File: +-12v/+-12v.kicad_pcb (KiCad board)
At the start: 2 copper layers, 83.3 x 65 mm, 33 parts, among them J1 Conn_01x04_Male, J2 Conn_01x03_Male, J3 Screw_Terminal_01x02, J4 Screw_Terminal_01x02, U1 LM317_TO3, U2 LM337_TO3

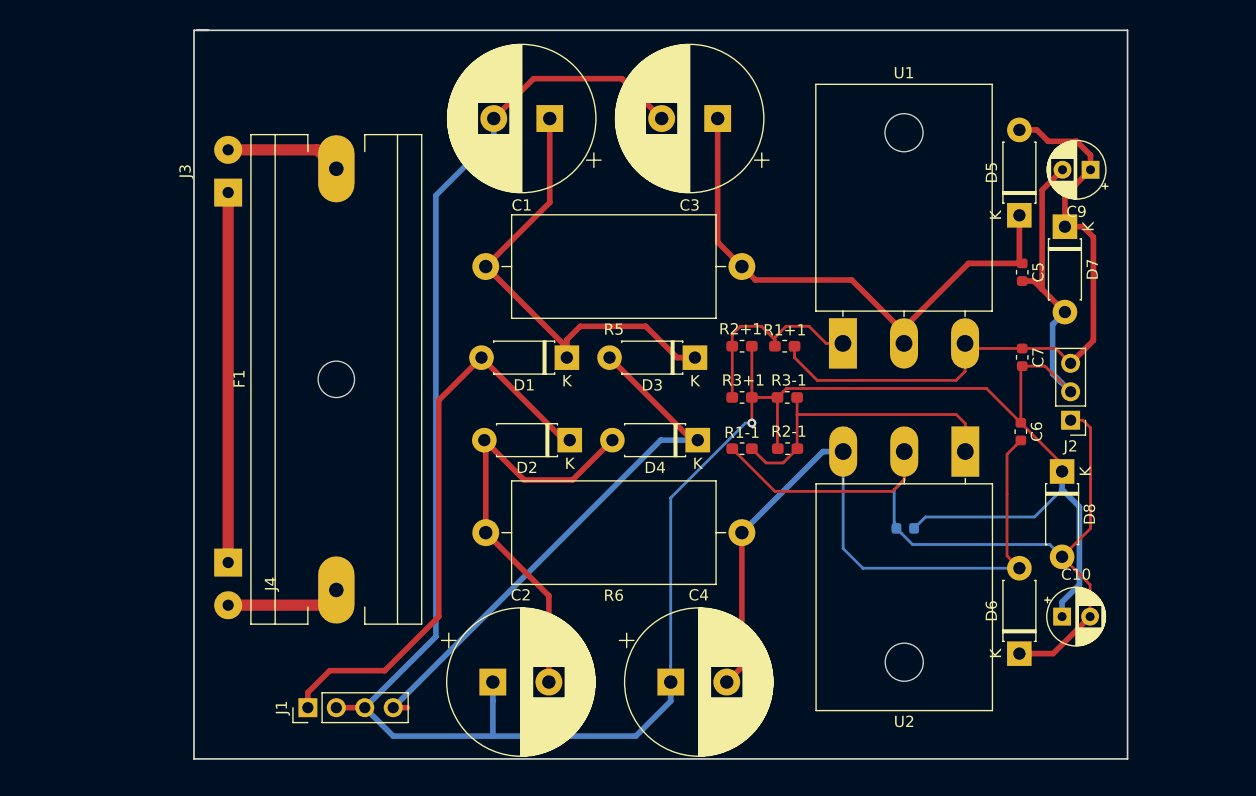
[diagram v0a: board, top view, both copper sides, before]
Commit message: Fix wrong fottprints (the expensive way)
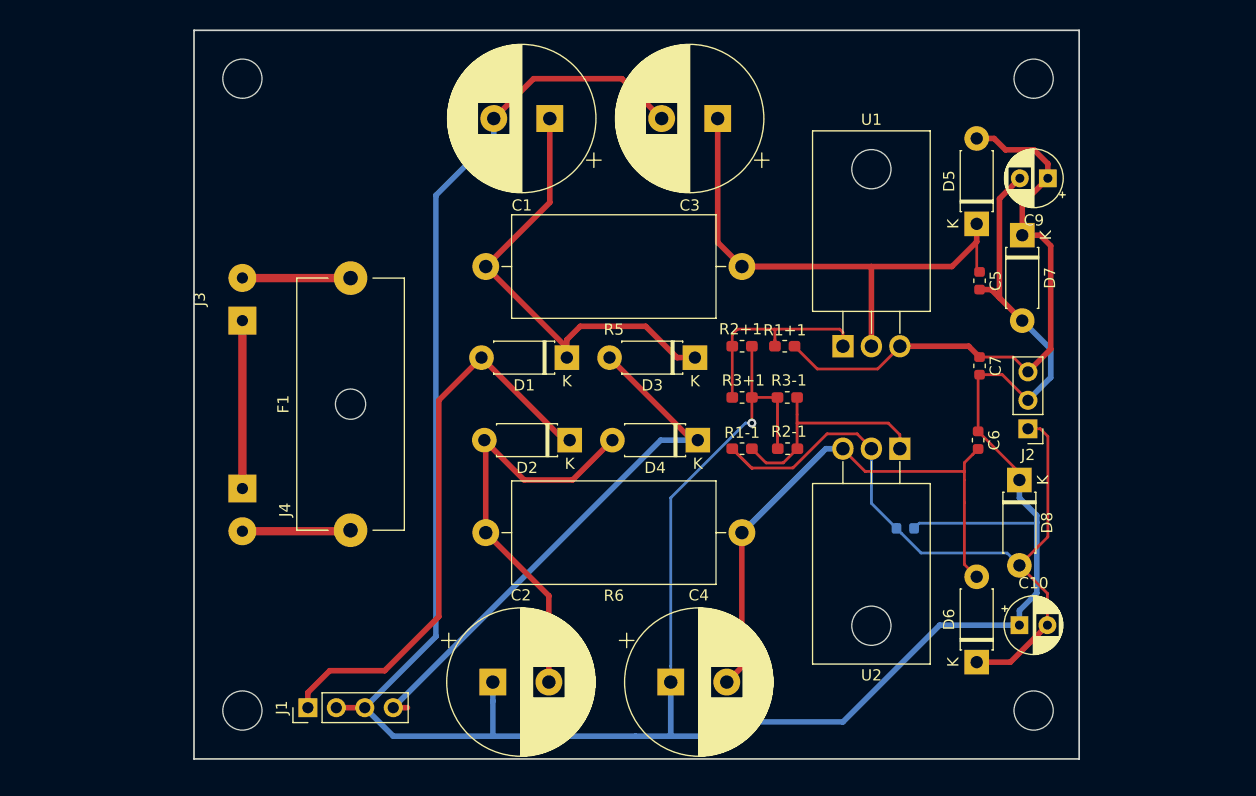
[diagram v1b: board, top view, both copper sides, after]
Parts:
- added REF**: MountingHole_3.5mm, MountingHole:MountingHole_3.5mm, F.Cu at (102.9, 74.4)
- added REF**: MountingHole_3.5mm, MountingHole:MountingHole_3.5mm, F.Cu at (32.3, 74.4)
- added REF**: MountingHole_3.5mm, MountingHole:MountingHole_3.5mm, F.Cu at (32.3, 130.8)
- added REF**: MountingHole_3.5mm, MountingHole:MountingHole_3.5mm, F.Cu at (102.9, 130.8)
- F1: footprint Fuse:Fuseholder_Cylinder-5x20mm_Schurter_0031-8002_Horizontal_Open -> Fuse:Fuseholder_Cylinder-5x20mm_Schurter_0031_8201_Horizontal_Open
- U1, U2: footprint Package_TO_SOT_THT:TO-3P-3_Horizontal_TabDown -> Package_TO_SOT_THT:TO-220F-3_Horizontal_TabDown
- moved J3 11.5 mm to (32.3, 96.0)
- moved J4 6.73 mm to (32.3, 111.0)
- moved U2 5.85 mm to (90.9, 107.4)
- moved F1 5.48 mm to (41.9, 114.7)
- moved C10 3.89 mm to (101.6, 123.2)
- moved C5 3.89 mm to (98.0, 92.5)
- moved C6 3.89 mm to (97.9, 106.7)
- moved C7 3.89 mm to (98.0, 100.1)
- moved C9 3.89 mm to (104.1, 83.3)
- moved D7 3.89 mm to (101.9, 88.4)
- moved D8 3.89 mm to (101.6, 110.2)
- moved J2 3.89 mm to (102.4, 105.7)
- moved D5 3.89 mm to (97.8, 87.4)
- moved D6 3.89 mm to (97.8, 126.5)
- moved U1 0.25 mm to (85.9, 98.3)
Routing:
- net Net-(J3-Pad1): track 33.0 -> 15.0 mm
- net /GND: track 247.2 -> 258.3 mm
- net Net-(R1-1-Pad2): track 27.5 -> 20.6 mm
- net Net-(C7-Pad1): track 59.7 -> 53.1 mm
- net Net-(C10-Pad2): track 71.7 -> 66.9 mm
- net Net-(C3-Pad1): track 50.7 -> 55.3 mm
- net Net-(C4-Pad2): track 63.4 -> 60.3 mm
- net Net-(F1-Pad2): track 10.4 -> 9.66 mm
- net Net-(F1-Pad1): track 10.2 -> 9.69 mm
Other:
- board size 83.3 x 65 mm -> 79 x 65 mm

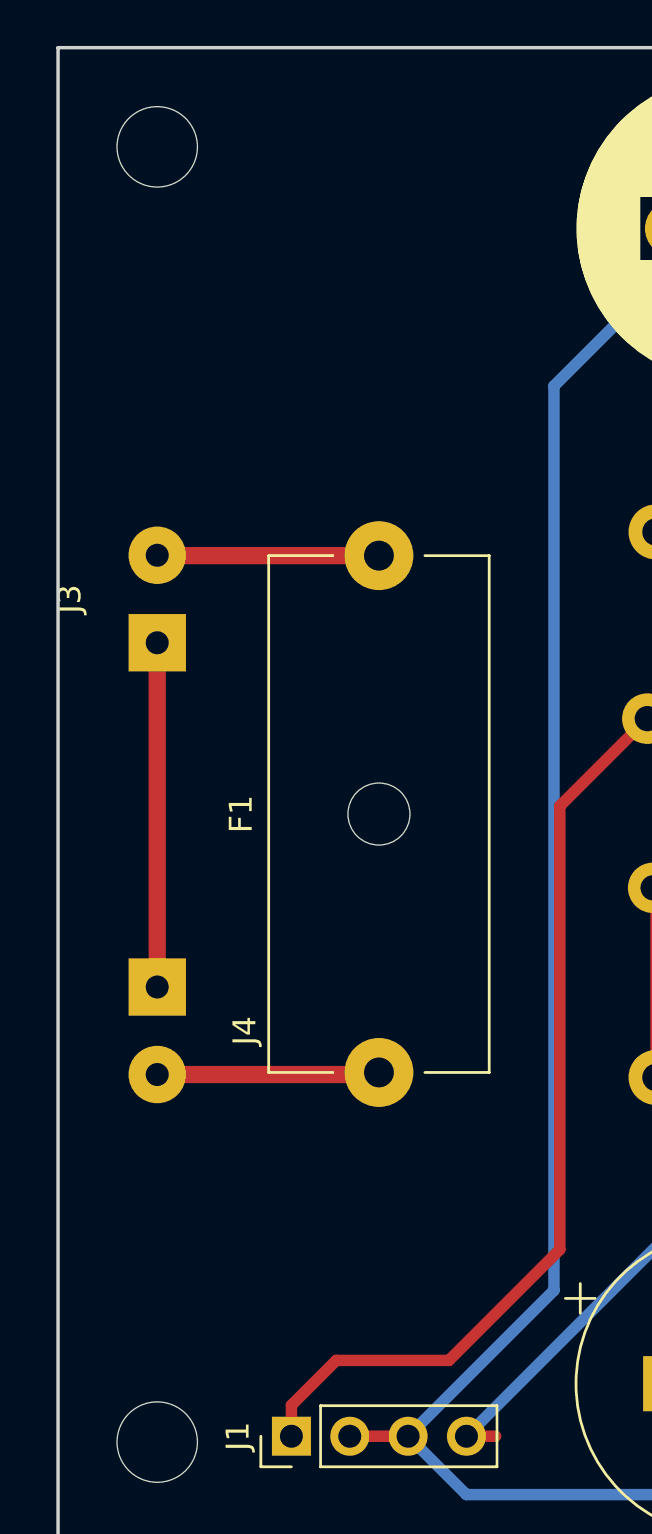
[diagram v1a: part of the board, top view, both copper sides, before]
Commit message: Fix Footprint for Reichelt relay
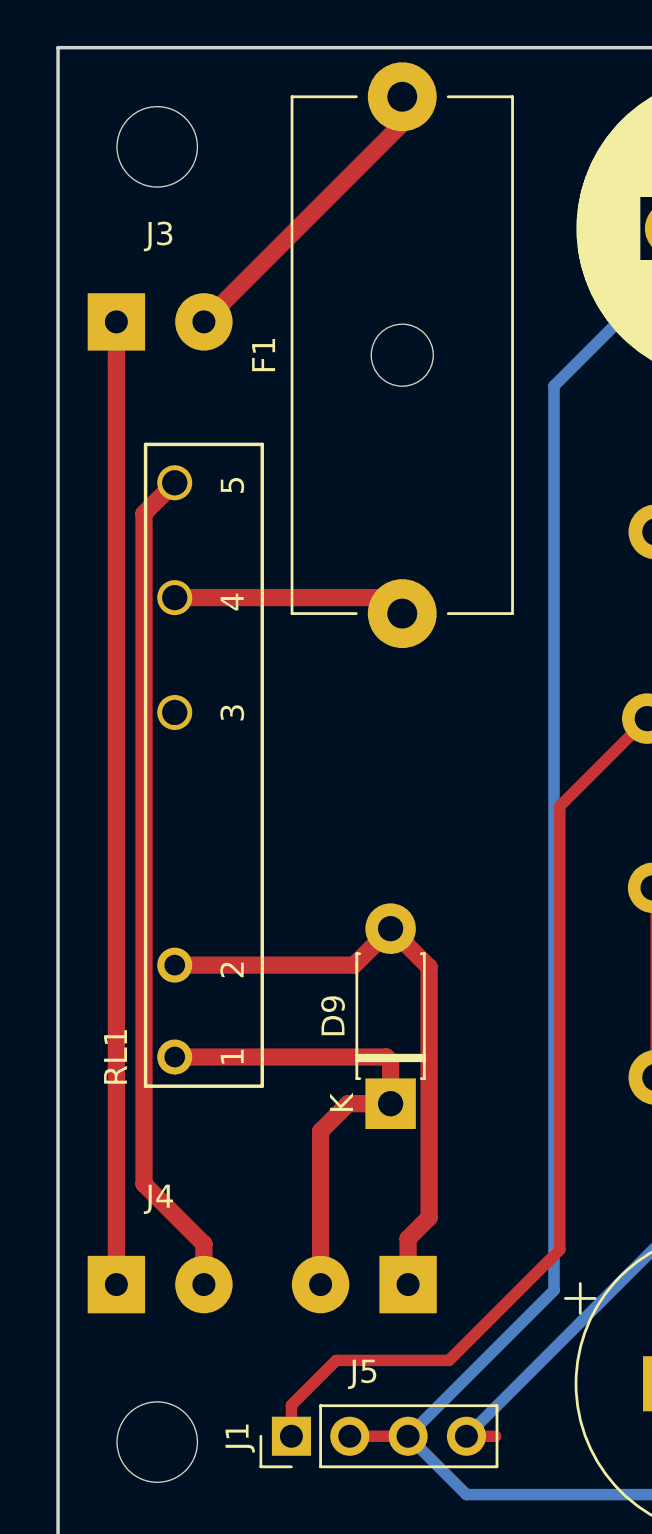
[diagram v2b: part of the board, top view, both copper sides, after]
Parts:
- added D9: D_Small, Diode_THT:D_DO-41_SOD81_P7.62mm_Horizontal, F.Cu at (42.4, 116.1)
- added J5: Screw_Terminal_01x02, Connector_Wire:SolderWirePad_1x02_P3.81mm_Drill1mm, F.Cu at (43.2, 124.0)
- added RL1: FTR-LYCA, lci-kicad:FTR-LYCA, F.Cu at (33.0, 114.0)
- moved F1 20.0 mm to (42.9, 94.7)
- moved J3 14.1 mm to (30.5, 82.0), turned to 0 degrees
- moved J4 13.1 mm to (30.5, 124.0), turned to 0 degrees
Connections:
- J4 pad 2: Net-(F1-Pad1) -> Net-(J4-Pad2)
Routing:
- net Net-(J4-Pad2): track 0.00 -> 36.5 mm
- net Net-(J3-Pad1): track 15.0 -> 41.9 mm
- net Net-(D9-Pad2): track 0.00 -> 26.6 mm
- net Net-(D9-Pad1): track 0.00 -> 21.5 mm
- net Net-(F1-Pad2): track 9.66 -> 15.1 mm
- net Net-(F1-Pad1): track 9.69 -> 10.2 mm

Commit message: New power connector and changes trickling out. Redid P2 in Kicad
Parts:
- removed REF** (x4): MountingHole_3.5mm, MountingHole:MountingHole_3.5mm
- added H1: MountingHole, MountingHole:MountingHole_3.2mm_M3_DIN965, F.Cu at (15.9, 74.3)
- added H2: MountingHole, MountingHole:MountingHole_3.2mm_M3_DIN965, F.Cu at (117.5, 74.3)
- added H3: MountingHole, MountingHole:MountingHole_3.2mm_M3_DIN965, F.Cu at (15.9, 133.0)
- added H4: MountingHole, MountingHole:MountingHole_3.2mm_M3_DIN965, F.Cu at (117.5, 133.0)
- added H5: MountingHole, MountingHole:MountingHole_3.2mm_M3_DIN965, F.Cu at (15.8, 91.2)
- added H6: MountingHole, MountingHole:MountingHole_3.2mm_M3_DIN965, F.Cu at (58.4, 74.2)
- added H7: MountingHole, MountingHole:MountingHole_3.2mm_M3_DIN965, F.Cu at (58.4, 90.8)
- added J6: Conn_02x05_Odd_Even, Connector_PinSocket_2.54mm:PinSocket_2x05_P2.54mm_Vertical, F.Cu at (30.8, 83.3)
- added U3: RECOM_RAC02-05SC, lci-kicad:RECOM_RAC02-05SC, F.Cu at (25.4, 109.5)
- J5: value Screw_Terminal_01x02 -> Conn_01x10; footprint Connector_Wire:SolderWirePad_1x02_P3.81mm_Drill1mm -> Connector_PinHeader_2.54mm:PinHeader_1x10_P2.54mm_Vertical
- moved J5 51.8 mm to (24.9, 75.4), turned to 90 degrees
- moved J3 50.4 mm to (39.6, 131.6)
- moved F1 33.9 mm to (57.7, 125.3)
- moved C1 13.8 mm to (73.4, 79.0)
- moved C10 13.8 mm to (115.3, 124.2)
- moved C5 13.8 mm to (111.8, 93.5)
- moved C7 13.8 mm to (111.8, 101.1)
- moved D1 13.8 mm to (74.9, 100.3)
- moved D4 13.8 mm to (86.6, 107.7)
- moved D8 13.8 mm to (115.3, 111.3)
- moved J2 13.8 mm to (116.1, 106.7)
- moved R2-1 13.8 mm to (94.6, 108.5)
- moved R5 13.8 mm to (90.6, 92.2)
- moved R6 13.8 mm to (90.6, 116.0)
- moved J1 13.8 mm to (51.8, 131.6)
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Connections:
- net Net-(D9-Pad2) renamed /DGND
- C10 pad 2: Net-(C10-Pad2) -> /-12v
- C7 pad 1: Net-(C7-Pad1) -> /+12v
- C8 pad 2: Net-(C10-Pad2) -> /-12v
- C9 pad 1: Net-(C7-Pad1) -> /+12v
- D5 pad 2: Net-(C7-Pad1) -> /+12v
- D6 pad 1: Net-(C10-Pad2) -> /-12v
- D7 pad 1: Net-(C7-Pad1) -> /+12v
- D8 pad 2: Net-(C10-Pad2) -> /-12v
- J2 pad 1: Net-(C10-Pad2) -> /-12v
- J2 pad 3: Net-(C7-Pad1) -> /+12v
- J3 pad 2: Net-(F1-Pad2) -> Net-(F1-Pad1)
- J5 pad 2: Net-(D9-Pad1) -> /+5v
- R1+1 pad 2: Net-(C7-Pad1) -> /+12v
- R1-1 pad 1: Net-(C10-Pad2) -> /-12v
- RL1 pad 3: (no net) -> Net-(RL1-Pad3)
- RL1 pad 4: Net-(F1-Pad1) -> Net-(F1-Pad2)
- U1 pad 3: Net-(C7-Pad1) -> /+12v
- U2 pad 2: Net-(C10-Pad2) -> /-12v
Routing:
- net /+12v: track 0.00 -> 147.7 mm
- net Net-(C10-Pad2): track 66.9 -> 0.00 mm
- net /-12v: track 0.00 -> 66.9 mm
- net Net-(D9-Pad1): track 21.5 -> 81.9 mm
- net Net-(C7-Pad1): track 53.1 -> 0.00 mm
- net Net-(F1-Pad1): track 10.2 -> 47.0 mm
- net /GND: track 258.3 -> 292.5 mm
- net /DGND: track 26.6 -> 59.2 mm
- net Net-(J3-Pad1): track 41.9 -> 19.7 mm
- net /+5v: track 0.00 -> 22.1 mm
- net Net-(J4-Pad2): track 36.5 -> 50.3 mm
- net Net-(F1-Pad2): track 15.1 -> 14.1 mm
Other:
- board size 79 x 65 mm -> 108 x 65 mm

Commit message: Sigh2.
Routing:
- net /-12v: track 66.9 -> 80.0 mm
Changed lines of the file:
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@@
-(kicad_pcb (version 20171130) (host pcbnew "(5.0.1-3-g963ef8bb5)")
+(kicad_pcb (version 20171130) (host pcbnew "(5.1.5-0-10_14)")
   (general
     (thickness 1.6)
     (drawings 8)
-    (tracks 233)
+    (tracks 235)
     (zones 0)
     (modules 45)
@@
     (zone_45_only no)
     (trace_min 0.2)
-    (segment_width 0.2)
-    (edge_width 0.15)
     (via_size 0.8)
     (via_drill 0.4)
@@
     (uvia_min_size 0.2)
     (uvia_min_drill 0.1)
+    (edge_width 0.15)
+    (segment_width 0.2)
     (pcb_text_width 0.3)
     (pcb_text_size 1.5 1.5)
@@
   (segment (start 84.074 134.112) (end 81.075 134.112) (width 0.5) (layer B.Cu) (net 10))
   (segment (start 63.246 96.774) (end 63.246 125.222) (width 0.5) (layer B.Cu) (net 10))
-  (segment (start 48.768 78.994) (end 68.406 78.994) (width 0.5) (layer F.Cu) (net 10))
-  (segment (start 45.212 75.438) (end 48.768 78.994) (width 0.5) (layer F.Cu) (net 10))
   (segment (start 71.962 75.438) (end 79.836 75.438) (width 0.5) (layer F.Cu) (net 10))
   (segment (start 79.836 75.438) (end 83.392 78.994) (width 0.5) (layer F.Cu) (net 10))
@@
   (segment (start 45.212 79.04988) (end 45.212 75.438) (width 0.5) (layer F.Cu) (net 10))
   (segment (start 41.00576 83.25612) (end 45.212 79.04988) (width 0.5) (layer F.Cu) (net 10))
+  (segment (start 48.768 78.994) (end 68.406 78.994) (width 0.5) (layer B.Cu) (net 10))
+  (segment (start 45.212 75.438) (end 48.768 78.994) (width 0.5) (layer B.Cu) (net 10))
   (segment (start 74.676 107.696) (end 75.184 107.696) (width 0.5) (layer F.Cu) (net 11))
   (segment (start 67.31 100.33) (end 74.676 107.696) (width 0.5) (layer F.Cu) (net 11))
@@
   (segment (start 106.545001 117.772001) (end 104.804612 116.031612) (width 0.25) (layer B.Cu) (net 16))
   (segment (start 115.316 118.872) (end 114.216001 117.772001) (width 0.25) (layer B.Cu) (net 16))
+  (segment (start 47.752 79.04988) (end 47.752 75.438) (width 0.5) (layer F.Cu) (net 16))
+  (segment (start 41.00576 85.79612) (end 47.752 79.04988) (width 0.5) (layer F.Cu) (net 16))
   (segment (start 43.752 111.062) (end 46.736 111.062) (width 0.5) (layer B.Cu) (net 17))
   (segment (start 42.164 109.474) (end 43.752 111.062) (width 0.5) (layer B.Cu) (net 17))
